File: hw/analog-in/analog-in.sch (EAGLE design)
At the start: 120 parts

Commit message: analog-in: add comments with PCB mistakes
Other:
- note added: "DIR_2 nicht verbunden. -> ID LED"
- note added: "I2C PULL UPs Fehlen"
- note added: "Part nr falsch"
- note added: "Pin 1 und pin 10 vertauscht!"
- note added: "move Bypass to output"
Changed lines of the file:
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@@
 <text x="279.4" y="228.6" size="1.778" layer="91">220kHz = 2.2k + 330p</text>
 <text x="116.84" y="271.78" size="1.778" layer="91">100mA, 250V</text>
+<text x="203.2" y="238.76" size="5.08" layer="88">Pin 1 und pin 10 vertauscht!</text>
+<text x="459.74" y="299.72" size="5.08" layer="88">Part nr falsch</text>
+<text x="160.02" y="193.04" size="5.08" layer="88">Part nr falsch</text>
+<text x="350.52" y="104.14" size="5.08" layer="88">Part nr falsch</text>
+<text x="525.78" y="335.28" size="5.08" layer="88">Part nr falsch</text>
+<text x="266.7" y="175.26" size="5.08" layer="88">Part nr falsch</text>
+<text x="401.32" y="73.66" size="5.08" layer="88">I2C PULL UPs Fehlen</text>
+<text x="467.36" y="104.14" size="5.08" layer="88">I2C PULL UPs Fehlen</text>
+<text x="233.68" y="81.28" size="5.08" layer="88">DIR_2 nicht verbunden. -&gt; ID LED</text>
+<text x="447.04" y="231.14" size="5.08" layer="88">move Bypass to output</text>
 </plain>
 <instances>

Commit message: hw/analog-in: add mistake comment
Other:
- note added: "INA und INB vertauscht"
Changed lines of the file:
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@@
 <text x="233.68" y="81.28" size="5.08" layer="88">DIR_2 nicht verbunden. -&gt; ID LED</text>
 <text x="447.04" y="231.14" size="5.08" layer="88">move Bypass to output</text>
+<text x="251.46" y="142.24" size="5.08" layer="88">INA und INB vertauscht</text>
 </plain>
 <instances>

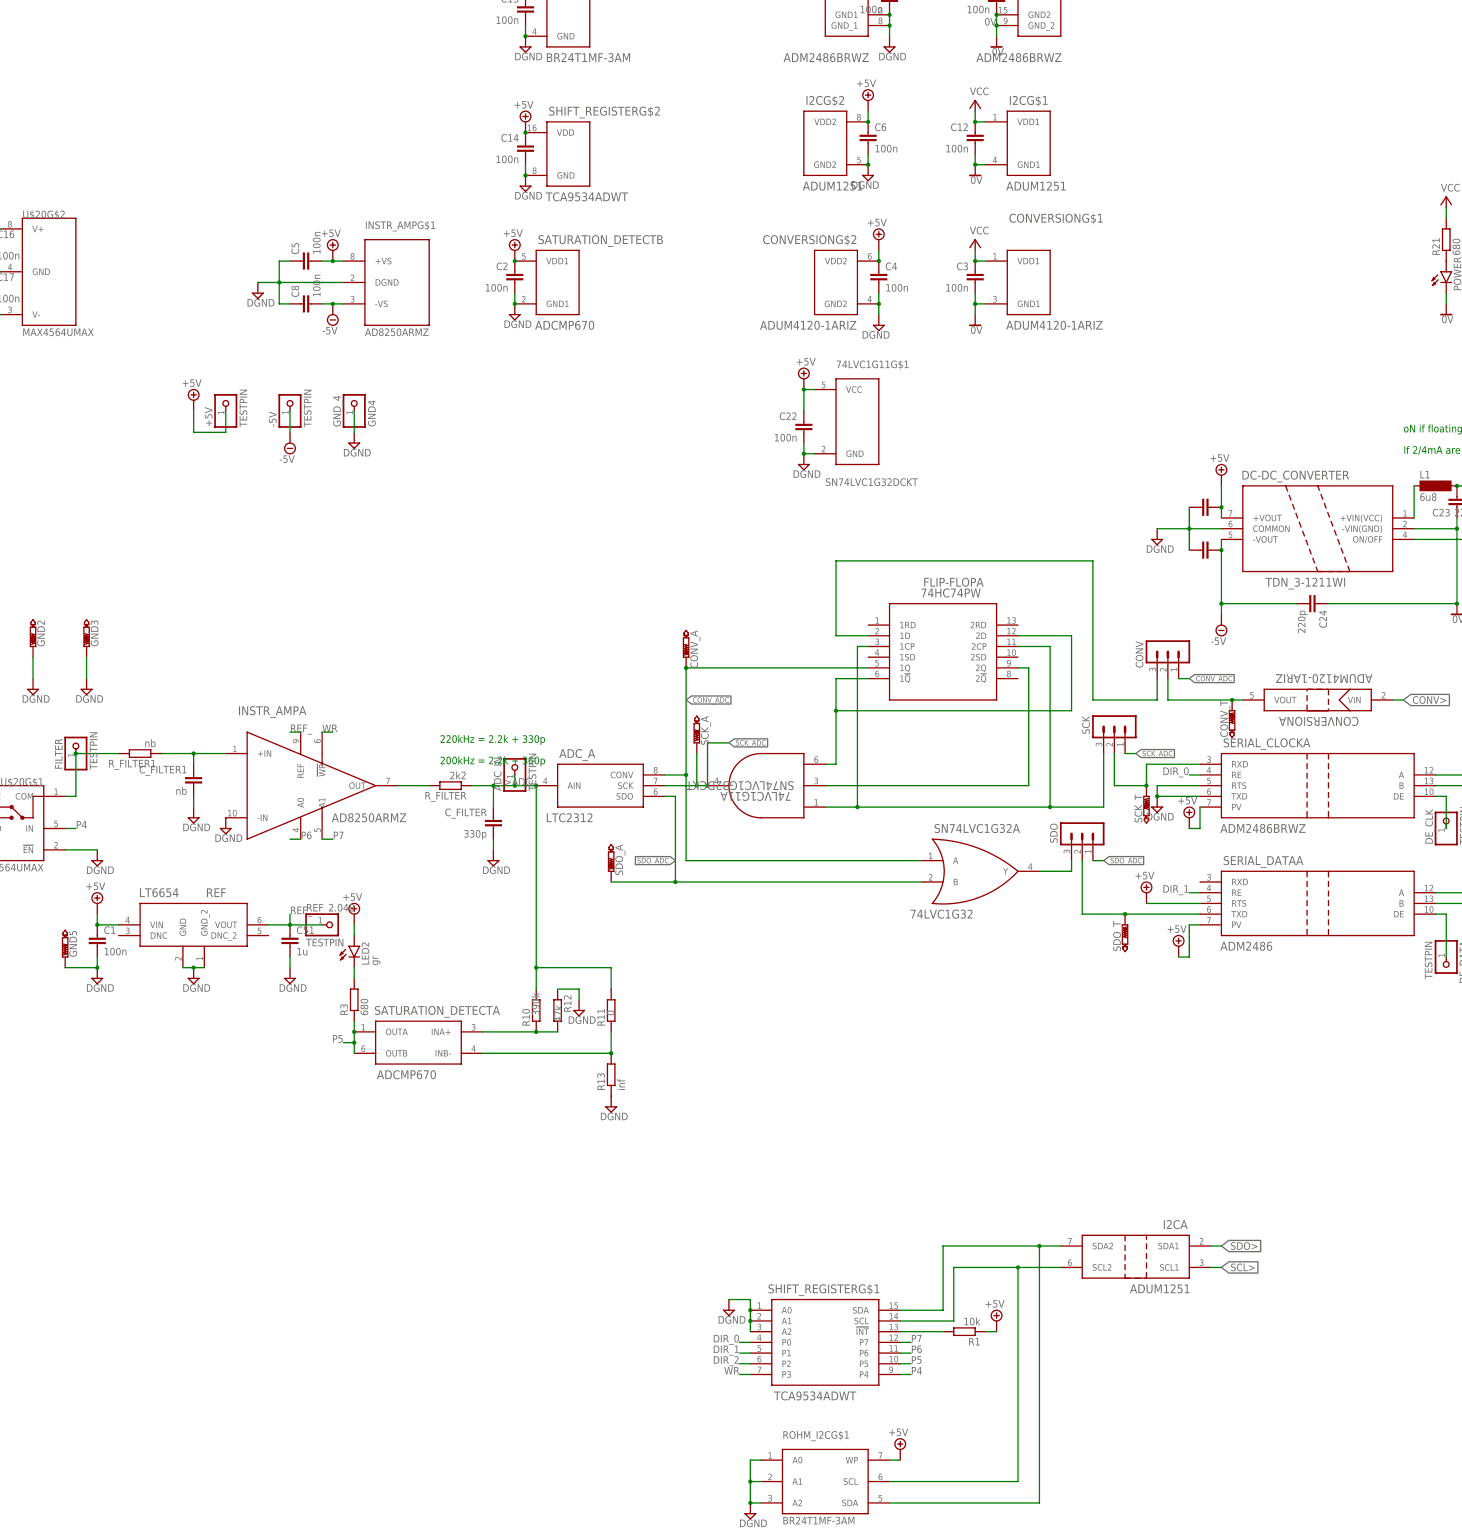
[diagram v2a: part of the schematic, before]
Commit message: hw/analog-in: fix mistakes from rev 1
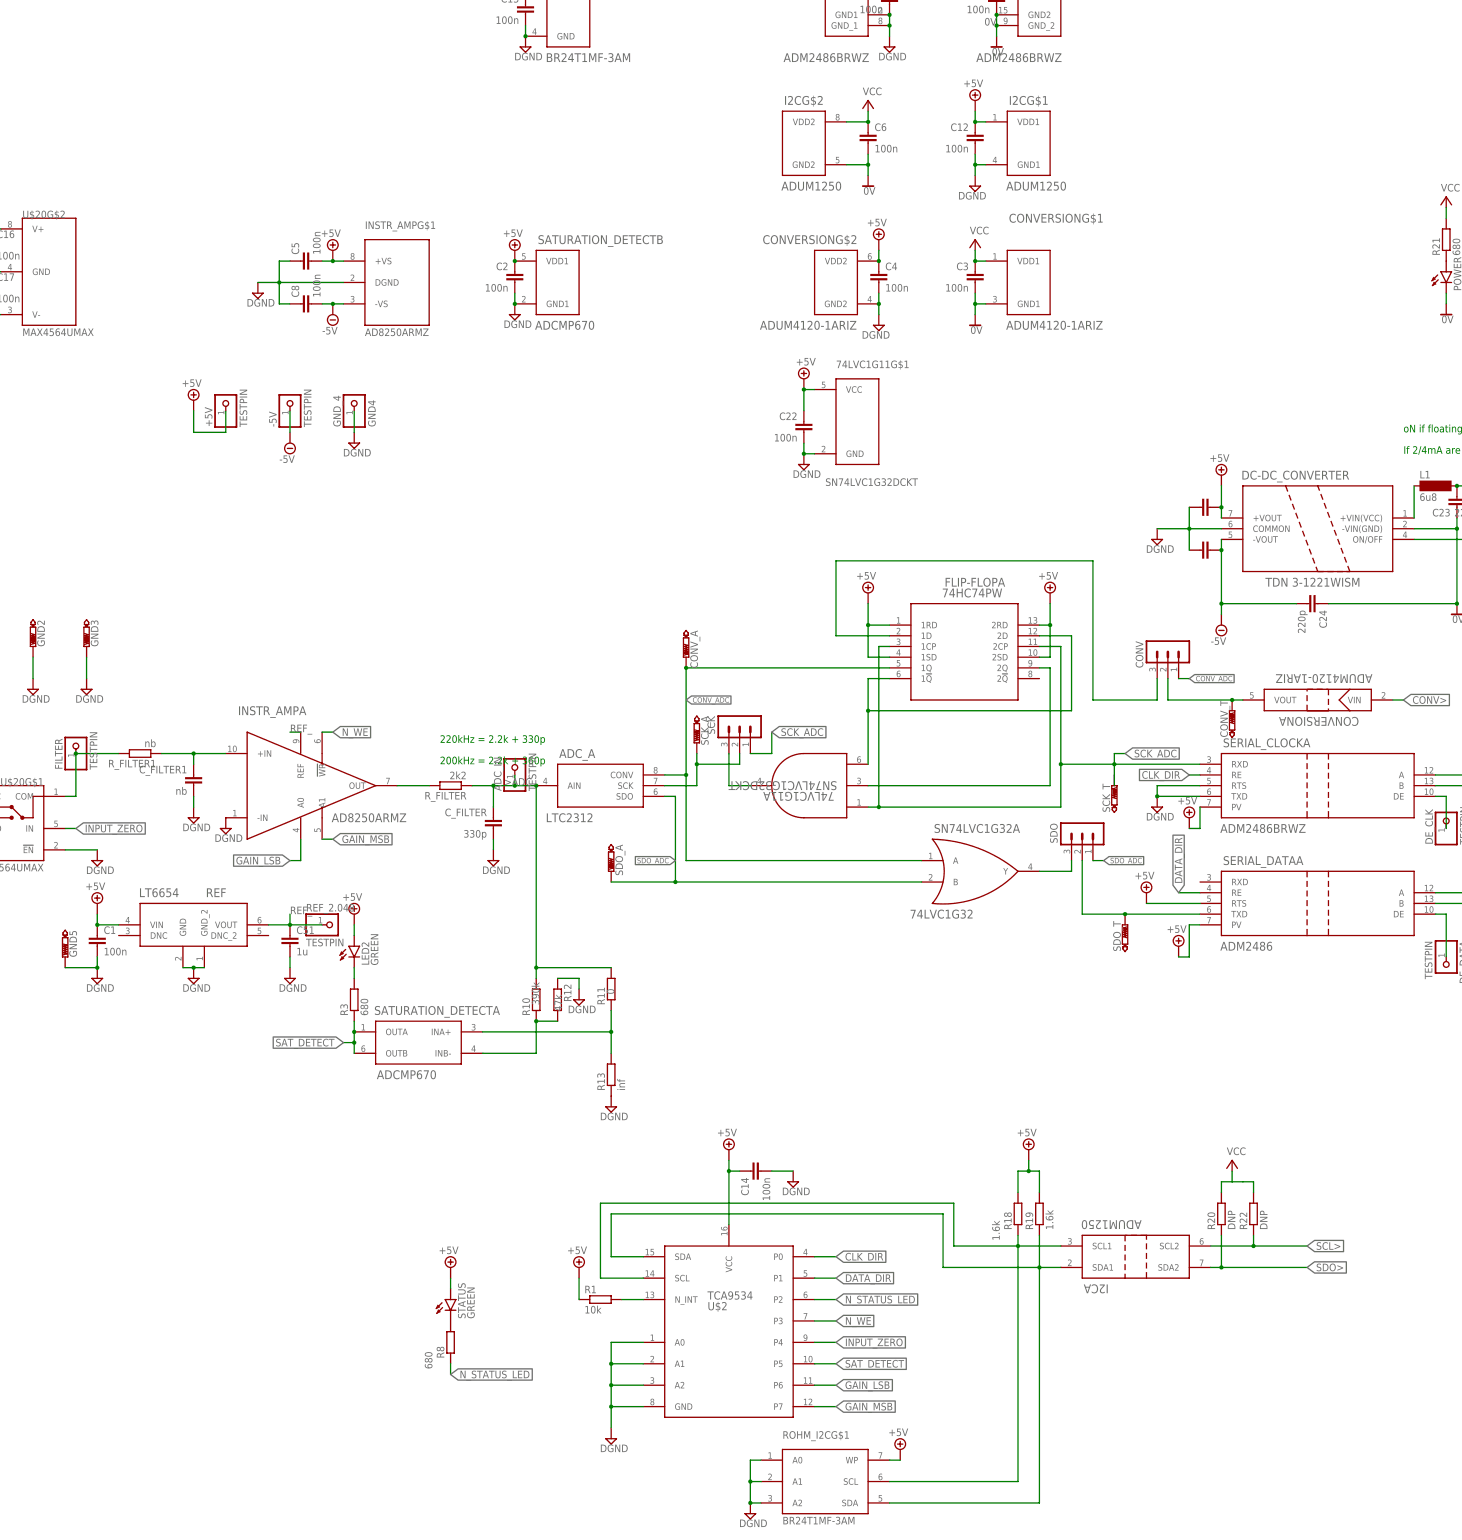
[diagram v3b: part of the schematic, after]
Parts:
- removed SHIFT_REGISTER: TCA9534ADWT, TCA9534ADWT:TCA9534ADWT
- added R18, R19: 1.6k, resistor:R-EU_R0805
- added R20, R22: DNP, resistor:R-EU_R0805
- added R8: 680, resistor:R-EU_R0805
- added STATUS: GREEN, led:LEDCHIPLED_0805
- added U$2: TCA9534, parts:TCA9534
- DC-DC_CONVERTER: value TDN_3-1211WI -> TDN 3-1221WISM; DIGIKEY TDN3-1211WISM-ND -> TDN3-1221WISM-ND; MANUFACTURER_PART_NUMBER (none) -> TDN 3-1221WISM
- I2C: value ADUM1251 -> ADUM1250
- INSTR_AMP: device AD8250:AD8250ARMZ -> parts:AD8250ARMZ
- LED2: value gr -> GREEN; DIGIKEY 754-1435-1-ND -> LTST-C170GKT; MOUSER 604-APT2012SGC -> (none)
- PIN_HEADER_SMD: DIGIKEY (none) -> 609-3487-2-ND
- POWER: DIGIKEY 754-1435-1-ND -> LTST-C170GKT; MOUSER 604-APT2012SGC -> (none)
- U$20: DIGIKEY MAX4565EAP+-ND -> MAX4564EUA+TR-ND
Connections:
- removed net DIR_0: SERIAL_CLOCKA.RE, SHIFT_REGISTERG$1.P0
- removed net DIR_1: SERIAL_DATAA.RE, SHIFT_REGISTERG$1.P1
- removed net DIR_2: SHIFT_REGISTERG$1.P2
- removed net N$28: SCK.2, SCK_T.TP, SERIAL_CLOCKA.RXD
- removed net P4: SHIFT_REGISTERG$1.P4, U$20G$1.IN
- removed net P5: R3.1, SATURATION_DETECTA.OUTA, SATURATION_DETECTA.OUTB, SHIFT_REGISTERG$1.P5
- removed net P6: INSTR_AMPA.A0, SHIFT_REGISTERG$1.P6
- removed net P7: INSTR_AMPA.A1, SHIFT_REGISTERG$1.P7
- removed net WR: INSTR_AMPA.!WR, SHIFT_REGISTERG$1.P3
- new net CLK_DIR: SERIAL_CLOCKA.RE, U$2.P0
- new net DATA_DIR: SERIAL_DATAA.RE, U$2.P1
- new net GAIN_LSB: INSTR_AMPA.A0, U$2.P6
- new net GAIN_MSB: INSTR_AMPA.A1, U$2.P7
- new net INPUT_ZERO: U$2.P4, U$20G$1.IN
- new net N$26: R8.2, STATUS.C
- new net N_STATUS_LED: R8.1, U$2.P2
- new net N_WE: INSTR_AMPA.!WR, U$2.P3
- new net SAT_DETECT: R3.1, SATURATION_DETECTA.OUTA, SATURATION_DETECTA.OUTB, U$2.P5
- net +5V: now also C12.1, FLIP-FLOPA.1RD, FLIP-FLOPA.1SD, FLIP-FLOPA.2RD, FLIP-FLOPA.2SD, I2CG$1.VDD1, R18.2, R19.2, STATUS.A, U$2.VCC; no longer C6.1, I2CG$2.VDD2, SHIFT_REGISTERG$2.VDD
- net 0V: now also C6.2, I2CG$2.GND2; no longer C12.2, I2CG$1.GND1
- net DGND: now also C12.2, I2CG$1.GND1, U$2.A0, U$2.A1, U$2.A2, U$2.GND; no longer C6.2, I2CG$2.GND2, SHIFT_REGISTERG$1.A0, SHIFT_REGISTERG$1.A1, SHIFT_REGISTERG$1.A2, SHIFT_REGISTERG$2.GND
- net N$13: now also 74LVC1G11A.Y; no longer 74LVC1G11A.A, FLIP-FLOPA.1CP, FLIP-FLOPA.2CP
- net N$17: now also SATURATION_DETECTA.INB-; no longer SATURATION_DETECTA.INA+
- net N$18: now also SATURATION_DETECTA.INA+; no longer SATURATION_DETECTA.INB-
- net N$2: now also U$2.N_INT; no longer SHIFT_REGISTERG$1.!INT
- net N$4: now also I2CA.SCL1, R18.1, U$2.SCL; no longer I2CA.SCL2, SHIFT_REGISTERG$1.SCL
- net N$6: now also I2CA.SDA1, R19.1, U$2.SDA; no longer I2CA.SDA2, SHIFT_REGISTERG$1.SDA
- net SCK_ADC: now also 74LVC1G11A.A, FLIP-FLOPA.1CP, FLIP-FLOPA.2CP, SCK.2, SCK_T.TP, SERIAL_CLOCKA.RXD; no longer 74LVC1G11A.Y
- net SCL>: now also I2CA.SCL2, R22.1; no longer I2CA.SCL1
- net SDO>: now also I2CA.SDA2, R20.1; no longer I2CA.SDA1
- net V+: now also C6.1, I2CG$2.VDD2, R20.2, R22.2; no longer C12.1, I2CG$1.VDD1
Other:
- note removed: "DIR_2 nicht verbunden. -> ID LED"
- note removed: "I2C PULL UPs Fehlen"
- note removed: "INA und INB vertauscht"
- note removed: "Part nr falsch"
- note removed: "Pin 1 und pin 10 vertauscht!"
- note removed: "move Bypass to output"
- moved on the sheet: 74LVC1G11A, C14, FLIP-FLOPA, I2CA, I2CG$2, R1, R10, R11, R12, SCK, SCK_T

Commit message: ADC board fixes
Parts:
- removed PIN_HEADER_SMD: (no value), SMD10_2_pinheader:MA05-2
- added CONV1: PTR1B1,27, testpad:PTR1B1,27
- added POWER1: gr, led:LEDSML0805
- added R23: 680, resistor:R-EU_R0805
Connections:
- removed net CONV<: PIN_HEADER_SMD.6, RJ45.5
- removed net CONV>: CONVERSIONA.VIN, PIN_HEADER_SMD.1
- removed net N_STATUS_LED: R8.1, U$2.P2
- removed net SCL<: PIN_HEADER_SMD.5, RJ45.7
- removed net SCL>: I2CA.SCL2, PIN_HEADER_SMD.2, R22.1
- removed net SDO<: PIN_HEADER_SMD.4, RJ45.8
- removed net SDO>: I2CA.SDA2, PIN_HEADER_SMD.3, R20.1
- new net CONV: CONV1.TP, CONVERSIONA.VIN, RJ45.5
- new net N$22: R8.1, STATUS.A
- new net N$27: POWER1.A, R23.1
- new net SCL: I2CA.SCL2, R22.1, RJ45.7
- new net SDO: I2CA.SDA2, R20.1, RJ45.8
- new net STATUS_LED: R8.2, U$2.P2
- net +5V: now also R23.2; no longer STATUS.A
- net DGND: now also POWER1.C, STATUS.C
- net N$26: now also ADC_A.SCK, SCK.2, SCK_A.TP; no longer R8.2, STATUS.C
- net SCK_ADC: no longer ADC_A.SCK, SCK.2, SCK_A.TP
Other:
- moved on the sheet: R8, SCK, SCK_A

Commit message: hw/analog-in: update schematics for analog in
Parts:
- R_FILTER1: value nb -> 0
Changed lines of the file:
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@@
 <attribute name="DIGIKEY" value="732-5316-ND"/>
 </part>
-<part name="R_FILTER1" library="rcl" library_urn="urn:adsk.eagle:library:334" deviceset="R-EU_" device="R0805" package3d_urn="urn:adsk.eagle:package:23553/2" value="nb">
+<part name="R_FILTER1" library="rcl" library_urn="urn:adsk.eagle:library:334" deviceset="R-EU_" device="R0805" package3d_urn="urn:adsk.eagle:package:23553/2" value="0">
 <spice>
 <pinmapping spiceprefix="R">

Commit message: hw/analog-in: add note
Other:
- note added: "WRONG FOOTPRINT L1"
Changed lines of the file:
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@@
 <text x="279.4" y="228.6" size="1.778" layer="91">220kHz = 2.2k + 330p</text>
 <text x="116.84" y="271.78" size="1.778" layer="91">100mA, 250V</text>
+<text x="508" y="289.56" size="1.778" layer="88">WRONG FOOTPRINT L1</text>
 </plain>
 <instances>

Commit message: hw: change isolator to si8400ab
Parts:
- I2C: value ADUM1250 -> SI8400AB-B-IS
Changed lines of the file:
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@@
 <attribute name="DIGIKEY" value="478-7962-1-ND"/>
 </part>
-<part name="I2C" library="ADUM1251WARZ" deviceset="ADUM1251WARZ" device="" value="ADUM1250">
+<part name="I2C" library="ADUM1251WARZ" deviceset="ADUM1251WARZ" device="" value="SI8400AB-B-IS">
 <attribute name="DIGIKEY" value="ADUM1251ARZ-RL7TR-ND"/>
 </part>
